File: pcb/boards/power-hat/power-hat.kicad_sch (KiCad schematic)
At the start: 40 parts, among them J1 ISO_A, J2 Raspberry_Pi_GPIO, J3 ISP, J4 FAN, Q1 IRLB8721PBF, Q2 2N7002, Q3 2N7002, U1 TPS54560BDDA, U2 LTV-817S, U3 attiny85, Y1 16Mhz Crystal

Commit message: Power HAT: Initial PCB layout with component placement
PCB Layout:
- 65mm × 56mm board outline (standard Pi HAT)
- 4× M2.5 mounting holes at corners
- 40-pin GPIO header (J2) positioned for Pi stacking
- Power section (U1 TPS54560, L1, capacitors) on left side
- MCU section (U3 ATtiny85, Y1 crystal) in center
- MOSFET power switching (Q1, Q2, Q3) at bottom
- Optocoupler (U2) for ignition detection

Also includes:
- DAC/Amp HAT schematic complete with I2S, I2C, power wiring
- CAN HAT schematic updates
- Layout scripts for automated component placement
- Updated documentation

Co-Authored-By: Claude Opus 4.5 <noreply@anthropic.com>
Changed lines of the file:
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@@
 		(color 0 0 0 0)
 	)
-	(junction
-		(at 422.91 147.32)
-		(diameter 0)
-		(color 0 0 0 0)
-	)
 	(no_connect
 		(at 207.62 152.54)
@@
 	(wire
 		(pts
+			(xy 322.58 511.81) (xy 317.5 511.81)
+		)
+		(stroke
+			(width 0)
+			(type default)
+		)
+	)
+	(wire
+		(pts
 			(xy 172.72 121.92) (xy 182.88 121.92)
 		)
@@
 	(wire
 		(pts
+			(xy 273.05 502.92) (xy 269.24 502.92)
+		)
+		(stroke
+			(width 0)
+			(type default)
+		)
+	)
+	(wire
+		(pts
 			(xy 118.11 702.31) (xy 118.11 701.04)
 		)
@@
 	(wire
 		(pts
-			(xy 436.88 123.19) (xy 444.5 123.19)
+			(xy 273.05 495.3) (xy 274.32 495.3)
 		)
 		(stroke
@@
 	(wire
 		(pts
-			(xy 549.91 510.54) (xy 549.91 508)
+			(xy 436.88 123.19) (xy 444.5 123.19)
 		)
 		(stroke
@@
 	(wire
 		(pts
-			(xy 322.58 511.81) (xy 317.5 511.81)
+			(xy 549.91 510.54) (xy 549.91 508)
 		)
 		(stroke
@@
 	(wire
 		(pts
+			(xy 273.05 501.65) (xy 273.05 502.92)
+		)
+		(stroke
+			(width 0)
+			(type default)
+		)
+	)
+	(wire
+		(pts
 			(xy 628.65 576.58) (xy 628.65 574.04)
 		)
@@
 	(wire
 		(pts
+			(xy 273.05 500.38) (xy 269.24 500.38)
+		)
+		(stroke
+			(width 0)
+			(type default)
+		)
+	)
+	(wire
+		(pts
 			(xy 104.3 334.01) (xy 114.3 334.01)
 		)
@@
 	(wire
 		(pts
-			(xy 183 127.14) (xy 194.92 127.14)
+			(xy 273.05 495.3) (xy 273.05 500.38)
 		)
 		(stroke
@@
 	(wire
 		(pts
-			(xy 549.91 508) (xy 566.42 508)
+			(xy 183 127.14) (xy 194.92 127.14)
 		)
 		(stroke
@@
 	(wire
 		(pts
-			(xy 101.6 321.31) (xy 97.79 321.31)
+			(xy 549.91 508) (xy 566.42 508)
 		)
 		(stroke
@@
 	(wire
 		(pts
-			(xy 381 194.31) (xy 391 194.31)
+			(xy 101.6 321.31) (xy 97.79 321.31)
 		)
 		(stroke
@@
 	(wire
 		(pts
-			(xy 44.45 134.62) (xy 58.42 134.62)
+			(xy 381 194.31) (xy 391 194.31)
 		)
 		(stroke
@@
 	(wire
 		(pts
-			(xy 381 186.69) (xy 376 186.69)
+			(xy 273.05 501.65) (xy 276.86 501.65)
 		)
 		(stroke
@@
 	(wire
 		(pts
-			(xy 38.1 127) (xy 58.42 127)
+			(xy 44.45 134.62) (xy 58.42 134.62)
 		)
 		(stroke
@@
 	(wire
 		(pts
-			(xy 321.31 124.46) (xy 318.77 124.46)
+			(xy 381 186.69) (xy 376 186.69)
 		)
 		(stroke
@@
 	(wire
 		(pts
-			(xy 127 130.81) (xy 137 130.81)
+			(xy 38.1 127) (xy 58.42 127)
 		)
 		(stroke
@@
 	(wire
 		(pts
-			(xy 415.29 147.32) (xy 422.91 147.32)
+			(xy 321.31 124.46) (xy 318.77 124.46)
 		)
 		(stroke
@@
 	(wire
 		(pts
-			(xy 269.24 500.38) (xy 274.32 500.38)
+			(xy 127 130.81) (xy 137 130.81)
 		)
 		(stroke
@@
 	(wire
 		(pts
-			(xy 269.24 502.92) (xy 274.32 502.92)
+			(xy 415.29 147.32) (xy 422.91 147.32)
 		)
 		(stroke
@@
 		)
 	)
+	(global_label "HEARTBEAT_LED"
+		(shape input)
+		(at 274.32 495.3 0)
+		(fields_autoplaced yes)
+		(effects
+			(font
+				(size 1.27 1.27)
+			)
+			(justify left)
+		)
+		(property "Intersheetrefs" "${INTERSHEET_REFS}"
+			(at 274.32 495.3 0)
+			(effects
+				(font
+					(size 1.27 1.27)
+				)
+				(hide yes)
+			)
+		)
+	)
 	(global_label "+5V"
 		(shape passive)
@@
 		)
 	)
+	(global_label "Q2_GATE"
+		(shape input)
+		(at 444.5 194.31 0)
+		(fields_autoplaced yes)
+		(effects
+			(font
+				(size 1.27 1.27)
+			)
+			(justify left)
+		)
+		(property "Intersheetrefs" "${INTERSHEET_REFS}"
+			(at 444.5 194.31 0)
+			(effects
+				(font
+					(size 1.27 1.27)
+				)
+				(hide yes)
+			)
+		)
+	)
 	(global_label "12V_FUSED"
 		(shape input)
@@
 		)
 	)
+	(global_label "R6_OUT"
+		(shape input)
+		(at 322.58 511.81 0)
+		(fields_autoplaced yes)
+		(effects
+			(font
+				(size 1.27 1.27)
+			)
+			(justify left)
+		)
+		(property "Intersheetrefs" "${INTERSHEET_REFS}"
+			(at 322.58 511.81 0)
+			(effects
+				(font
+					(size 1.27 1.27)
+				)
+				(hide yes)
+			)
+		)
+	)
 	(global_label "GND"
 		(shape passive)
@@
 		)
 	)
+	(global_label "TIMER_LED"
+		(shape input)
+		(at 276.86 501.65 0)
+		(fields_autoplaced yes)
+		(effects
+			(font
+				(size 1.27 1.27)
+			)
+			(justify left)
+		)
+		(property "Intersheetrefs" "${INTERSHEET_REFS}"
+			(at 276.86 501.65 0)
+			(effects
+				(font
+					(size 1.27 1.27)
+				)
+				(hide yes)
+			)
+		)
+	)
 	(global_label "GND"
 		(shape input)
@@
 		)
 	)
-	(global_label "HEARTBEAT_LED"
-		(shape input)
-		(at 274.32 500.38 0)
-		(fields_autoplaced yes)
-		(effects
-			(font
-				(size 1.27 1.27)
-			)
-			(justify left)
-		)
-		(property "Intersheetrefs" "${INTERSHEET_REFS}"
-			(at 274.32 500.38 0)
-			(effects
-				(font
-					(size 1.27 1.27)
-				)
-				(hide yes)
-			)
-		)
-	)
-	(global_label "TIMER_LED"
-		(shape input)
-		(at 274.32 502.92 0)
-		(fields_autoplaced yes)
-		(effects
-			(font
-				(size 1.27 1.27)
-			)
-			(justify left)
-		)
-		(property "Intersheetrefs" "${INTERSHEET_REFS}"
-			(at 274.32 502.92 0)
-			(effects
-				(font
-					(size 1.27 1.27)
-				)
-				(hide yes)
-			)
-		)
-	)
-	(global_label "Q2_GATE"
-		(shape input)
-		(at 444.5 194.31 0)
-		(fields_autoplaced yes)
-		(effects
-			(font
-				(size 1.27 1.27)
-			)
-			(justify left)
-		)
-		(property "Intersheetrefs" "${INTERSHEET_REFS}"
-			(at 444.5 194.31 0)
-			(effects
-				(font
-					(size 1.27 1.27)
-				)
-				(hide yes)
-			)
-		)
-	)
-	(global_label "R6_OUT"
-		(shape input)
-		(at 317.5 511.81 0)
-		(fields_autoplaced yes)
-		(effects
-			(font
-				(size 1.27 1.27)
-			)
-			(justify left)
-		)
-		(property "Intersheetrefs" "${INTERSHEET_REFS}"
-			(at 317.5 511.81 0)
-			(effects
-				(font
-					(size 1.27 1.27)
-				)
-				(hide yes)
-			)
-		)
-	)
 	(symbol
 		(lib_id "Device:C")
@@
 		(dnp no)
 		(property "Reference" "R4"
-			(at 317.5 503 0)
+			(at 313.69 501.396 0)
 			(effects
 				(font
@@
 		)
 		(property "Value" "2N7002"
-			(at 381 132 0)
+			(at 373.888 131.318 0)
 			(effects
 				(font
@@
 		(dnp no)
 		(property "Reference" "J2"
-			(at 200 120 0)
+			(at 200.914 116.84 0)
 			(effects
 				(font

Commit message: Power HAT: Add 4-pin PWM fan control (GPIO12/13)
- Upgrade J4 from 2-pin to 4-pin PWM fan connector
- Wire FAN_PWM (GPIO12) for Pi-controlled speed
- Wire FAN_TACH (GPIO13) for RPM feedback
- Add layout_power_hat_v3.py with X735-style 30mm fan placement
- ERC clean: 0 errors, 49 warnings

Co-Authored-By: Claude Opus 4.5 <noreply@anthropic.com>
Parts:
- J4: value FAN -> FAN_4PIN; footprint Connector_PinHeader_2.54mm:PinHeader_1x02_P2.54mm_Vertical -> Connector_PinHeader_2.54mm:PinHeader_1x04_P2.54mm_Vertical; symbol Connector_Generic:Conn_01x02 -> Connector_Generic:Conn_01x04
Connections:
- net FAN+: now also J4.2 (Pin_2); no longer J4.1 (Pin_1)
- net FAN-: no longer J4.2 (Pin_2)
- net FAN_PWM: now also J2.32 (Pin_32), J4.4 (Pin_4)
- net GND: now also J4.1 (Pin_1)
- net FAN_TACH: now reaches J2.33 (Pin_33)
- net FAN_TACH: now also J4.3 (Pin_3)
- no-connect marks 38 -> 36
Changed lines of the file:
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@@
 		(color 0 0 0 0)
 	)
+	(junction
+		(at 628.65 574.04)
+		(diameter 0)
+		(color 0 0 0 0)
+	)
 	(no_connect
 		(at 207.62 152.54)
@@
 	)
 	(no_connect
-		(at 207.62 165.24)
-	)
-	(no_connect
 		(at 194.92 152.54)
 	)
@@
 	)
 	(no_connect
-		(at 194.92 167.78)
-	)
-	(no_connect
 		(at 207.62 172.86)
 	)
@@
 	(wire
 		(pts
+			(xy 623.57 572.77) (xy 626.11 572.77)
+		)
+		(stroke
+			(width 0)
+			(type default)
+		)
+	)
+	(wire
+		(pts
 			(xy 114.3 695.96) (xy 119.38 695.96)
 		)
@@
 	(wire
 		(pts
+			(xy 628.65 574.04) (xy 629.92 574.04)
+		)
+		(stroke
+			(width 0)
+			(type default)
+		)
+	)
+	(wire
+		(pts
 			(xy 572.77 501.65) (xy 574.04 501.65)
 		)
@@
 	(wire
 		(pts
-			(xy 626.11 567.69) (xy 623.57 567.69)
+			(xy 621.03 576.58) (xy 629.92 576.58)
+		)
+		(stroke
+			(width 0)
+			(type default)
+		)
+	)
+	(wire
+		(pts
+			(xy 626.11 562.61) (xy 614.68 562.61)
 		)
 		(stroke
@@
 	(wire
 		(pts
+			(xy 207.62 165.24) (xy 212.62 165.24)
+		)
+		(stroke
+			(width 0)
+			(type default)
+		)
+	)
+	(wire
+		(pts
 			(xy 760.73 820.42) (xy 765.81 820.42)
 		)
@@
 	(wire
 		(pts
+			(xy 626.11 574.04) (xy 628.65 574.04)
+		)
+		(stroke
+			(width 0)
+			(type default)
+		)
+	)
+	(wire
+		(pts
 			(xy 250.19 123.19) (xy 250.19 127)
 		)
@@
 	(wire
 		(pts
+			(xy 621.03 568.96) (xy 629.92 568.96)
+		)
+		(stroke
+			(width 0)
+			(type default)
+		)
+	)
+	(wire
+		(pts
 			(xy 207.62 162.7) (xy 212.62 162.7)
 		)
@@
 	(wire
 		(pts
-			(xy 207.62 129.68) (xy 212.62 129.68)
+			(xy 194.92 167.78) (xy 189.92 167.78)
 		)
 		(stroke
@@
 	(wire
 		(pts
-			(xy 127 349.25) (xy 127 350.52)
+			(xy 207.62 129.68) (xy 212.62 129.68)
 		)
 		(stroke
@@
 	(wire
 		(pts
-			(xy 137.16 703.58) (xy 137.16 701.04)
+			(xy 127 349.25) (xy 127 350.52)
 		)
 		(stroke
@@
 	(wire
 		(pts
-			(xy 623.57 576.58) (xy 628.65 576.58)
+			(xy 137.16 703.58) (xy 137.16 701.04)
 		)
 		(stroke
@@
 	(wire
 		(pts
-			(xy 626.11 567.69) (xy 626.11 571.5)
+			(xy 626.11 562.61) (xy 626.11 571.5)
 		)
 		(stroke
@@
 	(wire
 		(pts
-			(xy 628.65 574.04) (xy 629.92 574.04)
+			(xy 581.66 513.08) (xy 574.04 513.08)
 		)
 		(stroke
@@
 	(wire
 		(pts
-			(xy 581.66 513.08) (xy 574.04 513.08)
+			(xy 762 833.12) (xy 762 829.31)
 		)
 		(stroke
@@
 	(wire
 		(pts
-			(xy 762 833.12) (xy 762 829.31)
+			(xy 207.62 142.38) (xy 212.62 142.38)
 		)
 		(stroke
@@
 	(wire
 		(pts
-			(xy 207.62 142.38) (xy 212.62 142.38)
+			(xy 273.05 495.3) (xy 273.05 500.38)
 		)
 		(stroke
@@
 	(wire
 		(pts
-			(xy 273.05 495.3) (xy 273.05 500.38)
+			(xy 183 127.14) (xy 194.92 127.14)
 		)
 		(stroke
@@
 	(wire
 		(pts
-			(xy 183 127.14) (xy 194.92 127.14)
+			(xy 549.91 508) (xy 566.42 508)
 		)
 		(stroke
@@
 	(wire
 		(pts
-			(xy 549.91 508) (xy 566.42 508)
+			(xy 101.6 321.31) (xy 97.79 321.31)
 		)
 		(stroke
@@
 	(wire
 		(pts
-			(xy 101.6 321.31) (xy 97.79 321.31)
+			(xy 621.03 567.69) (xy 621.03 568.96)
 		)
 		(stroke
@@
 	(wire
 		(pts
+			(xy 626.11 572.77) (xy 626.11 574.04)
+		)
+		(stroke
+			(width 0)
+			(type default)
+		)
+	)
+	(wire
+		(pts
 			(xy 44.45 134.62) (xy 58.42 134.62)
 		)
@@
 		)
 	)
+	(global_label "FAN_TACH"
+		(shape passive)
+		(at 623.57 572.77 180)
+		(effects
+			(font
+				(size 1.27 1.27)
+			)
+			(justify right)
+		)
+		(property "Intersheetrefs" "${INTERSHEET_REFS}"
+			(at 623.57 572.77 0)
+			(effects
+				(font
+					(size 1.27 1.27)
+				)
+				(hide yes)
+			)
+		)
+	)
 	(global_label "GATE_CTRL"
 		(shape input)
@@
 		)
 	)
+	(global_label "FAN_PWM"
+		(shape passive)
+		(at 212.62 165.24 180)
+		(effects
+			(font
+				(size 1.27 1.27)
+			)
+			(justify right)
+		)
+		(property "Intersheetrefs" "${INTERSHEET_REFS}"
+			(at 212.62 165.24 0)
+			(effects
+				(font
+					(size 1.27 1.27)
+				)
+				(hide yes)
+			)
+		)
+	)
 	(global_label "GND"
 		(shape input)
@@
 		)
 	)
-	(global_label "XTAL1"
+	(global_label "GND"
+		(shape passive)
+		(at 621.03 567.69 180)
+		(effects
+			(font
+				(size 1.27 1.27)
+			)
+			(justify right)
+		)
+		(property "Intersheetrefs" "${INTERSHEET_REFS}"
+			(at 621.03 567.69 0)
+			(effects
+				(font
+					(size 1.27 1.27)
+				)
+				(hide yes)
+			)
+		)
+	)
+	(global_label "FAN_TACH"
 		(shape input)
-		(at 571.5 758.19 0)
-		(fields_autoplaced yes)
+		(at 189.92 167.78 0)
 		(effects
 			(font
@@
 		)
 		(property "Intersheetrefs" "${INTERSHEET_REFS}"
-			(at 571.5 758.19 0)
+			(at 189.92 167.78 0)
 			(effects
 				(font
@@
 		)
 	)
-	(global_label "FAN-"
+	(global_label "XTAL1"
 		(shape input)
-		(at 623.57 576.58 0)
+		(at 571.5 758.19 0)
 		(fields_autoplaced yes)
 		(effects
@@
 		)
 		(property "Intersheetrefs" "${INTERSHEET_REFS}"
-			(at 623.57 576.58 0)
+			(at 571.5 758.19 0)
 			(effects
 				(font
@@
 		)
 	)
+	(global_label "FAN_PWM"
+		(shape passive)
+		(at 621.03 576.58 180)
+		(effects
+			(font
+				(size 1.27 1.27)
+			)
+			(justify right)
+		)
+		(property "Intersheetrefs" "${INTERSHEET_REFS}"
+			(at 621.03 576.58 0)
+			(effects
+				(font
+					(size 1.27 1.27)
+				)
+				(hide yes)
+			)
+		)
+	)
 	(global_label "XTAL2"
 		(shape input)
@@
 	(global_label "FAN+"
 		(shape passive)
-		(at 623.57 567.69 0)
+		(at 614.68 562.61 0)
 		(effects
 			(font
@@
 		)
 		(property "Intersheetrefs" "${INTERSHEET_REFS}"
-			(at 623.57 567.69 0)
+			(at 614.68 562.61 0)
 			(effects
 				(font
@@
 	)
 	(symbol
-		(lib_id "Connector_Generic:Conn_01x02")
+		(lib_id "Connector_Generic:Conn_01x04")
 		(at 635 571.5 0)
 		(unit 1)
@@
 			)
 		)
-		(property "Value" "FAN"
+		(property "Value" "FAN_4PIN"
 			(at 635 576.5 0)
 			(effects
@@
 			)
 		)
-		(property "Footprint" "Connector_PinHeader_2.54mm:PinHeader_1x02_P2.54mm_Vertical"
+		(property "Footprint" "Connector_PinHeader_2.54mm:PinHeader_1x04_P2.54mm_Vertical"
 			(at 635 571.5 0)
 			(effects
@@
 		(pin "1"
 		)
+		(pin "4"
+		)
+		(pin "3"
+		)
 		(instances

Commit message: Power HAT: Fix ERC errors - 0 errors, 55 warnings
Manual schematic fixes:
- J1: Updated to Molex Micro-Fit 3.0 6-pin connector
- C6: Fixed short - changed bottom pin from +3.3V to GND
- C8: Reconnected as feedforward cap (+5V to U1-FB)
- C9: Fixed net label from 12V_IGN to 12V_FUSED
- R6: Fixed label to 12V_IGN to GND (ignition divider)
- D1 (TVS): Moved away from J2, reconnected 12V_FUSED to GND
- Removed stray 12V_IGN label hidden behind U1
- Added PWR_FLAG to 12V_FUSED and +3.3V nets

All critical ERC errors resolved. Remaining 55 warnings are
non-critical (off-grid endpoints, dangling labels, same local/global).

Co-Authored-By: Claude Opus 4.5 <noreply@anthropic.com>
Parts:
- removed J1: ISO_A, Connector_Molex:Molex_Mini-Fit_Jr_5566-08A_2x04_P4.20mm_Vertical, symbol Connector_Generic:Conn_01x08
- added J1: Micro-Fit_3.0, Connector_Molex:Molex_Micro-Fit_3.0_43045-0612_2x03_P3.00mm_Vertical, symbol Connector_Generic:Conn_02x03_Odd_Even
- C8: value 10uF -> 47pF
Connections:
- net +3.3V: no longer C6.2, J2.1 (Pin_1)
- net +5V: now also C8.1
- net 12V_ACC: now also J1.3 (Pin_3)
- net 12V_FUSED: now also J2.1 (Pin_1); no longer D2.2 (A), F1.1, R6.1, U1.3 (EN)
- net GND: now also C6.2, J1.4 (Pin_4), J1.5 (Pin_5), J1.6 (Pin_6); no longer C8.2
- net XTAL2: no longer C8.1
- new net 12V_IGN: D2.2 (A), F1.1, J1.1 (Pin_1), J1.2 (Pin_2), R6.1, U1.3 (EN)
- new net U1-FB: C8.2
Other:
- moved on the sheet: D1

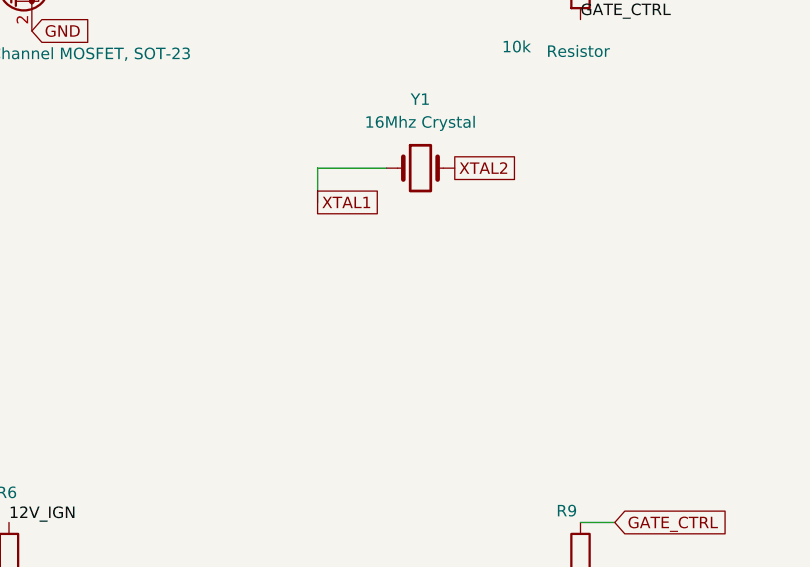
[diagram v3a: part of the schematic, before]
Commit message: Power HAT PCB: DRC clean routing via FreeRouting
- Complete auto-routing with FreeRouting (power-hat.ses)
- All DRC errors resolved (120 warnings, 0 errors)
- Fixed J2 +5V/GND short, edge clearance, R_COMP1 clearance
- Added keepout zone for fan cutout area
- Added STATUS.md with next steps (power trace widths need widening)

TODO: Widen power traces (12V_FUSED, +5V, GND, U1_SW) from 0.2mm to 1.5mm

Co-Authored-By: Claude Opus 4.5 <noreply@anthropic.com>
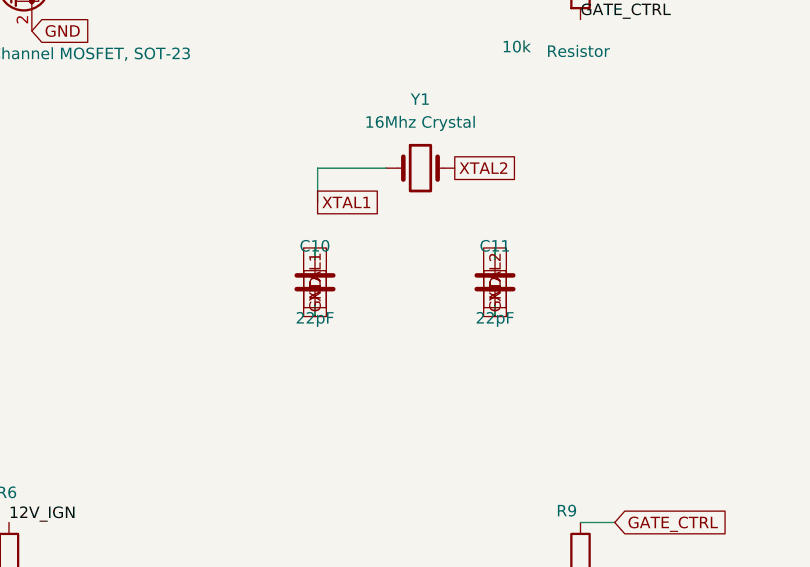
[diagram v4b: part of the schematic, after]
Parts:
- added C10, C11: 22pF, Capacitor_SMD:C_0805_2012Metric, symbol Device:C
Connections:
- net GND: now also C10.2, C11.2
- net XTAL1: now also C10.1
- net XTAL2: now also C11.1
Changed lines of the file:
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@@
 	)
 	(embedded_fonts no)
+	(symbol
+		(lib_id "Device:C")
+		(at 415.0 160.0 0)
+		(unit 1)
+		(exclude_from_sim no)
+		(in_bom yes)
+		(on_board yes)
+		(dnp no)
+		(property "Reference" "C10"
+			(at 415.0 156.0 0)
+			(effects
+				(font
+					(size 1.27 1.27)
+				)
+			)
+		)
+		(property "Value" "22pF"
+			(at 415.0 164.0 0)
+			(effects
+				(font
+					(size 1.27 1.27)
+				)
+			)
+		)
+		(property "Footprint" "Capacitor_SMD:C_0805_2012Metric"
+			(at 415.0 160.0 0)
+			(effects
+				(font
+					(size 1.27 1.27)
+				)
+				(hide yes)
+			)
+		)
+		(property "Datasheet" "~"
+			(at 415.0 160.0 0)
+			(effects
+				(font
+					(size 1.27 1.27)
+				)
+				(hide yes)
+			)
+		)
+		(property "Description" "Crystal load capacitor"
+			(at 415.0 160.0 0)
+			(effects
+				(font
+					(size 1.27 1.27)
+				)
+				(hide yes)
+			)
+		)
+		(pin "1"
+		)
+		(pin "2"
+		)
+		(instances
+			(project "power-hat"
+				(path "/29b54e26-6a52-4b51-8c39-076401b40ee9"
+					(reference "C10")
+					(unit 1)
+				)
+			)
+		)
+	)
+	(symbol
+		(lib_id "Device:C")
+		(at 435.0 160.0 0)
+		(unit 1)
+		(exclude_from_sim no)
+		(in_bom yes)
+		(on_board yes)
+		(dnp no)
+		(property "Reference" "C11"
+			(at 435.0 156.0 0)
+			(effects
+				(font
+					(size 1.27 1.27)
+				)
+			)
+		)
+		(property "Value" "22pF"
+			(at 435.0 164.0 0)
+			(effects
+				(font
+					(size 1.27 1.27)
+				)
+			)
+		)
+		(property "Footprint" "Capacitor_SMD:C_0805_2012Metric"
+			(at 435.0 160.0 0)
+			(effects
+				(font
+					(size 1.27 1.27)
+				)
+				(hide yes)
+			)
+		)
+		(property "Datasheet" "~"
+			(at 435.0 160.0 0)
+			(effects
+				(font
+					(size 1.27 1.27)
+				)
+				(hide yes)
+			)
+		)
+		(property "Description" "Crystal load capacitor"
+			(at 435.0 160.0 0)
+			(effects
+				(font
+					(size 1.27 1.27)
+				)
+				(hide yes)
+			)
+		)
+		(pin "1"
+		)
+		(pin "2"
+		)
+		(instances
+			(project "power-hat"
+				(path "/29b54e26-6a52-4b51-8c39-076401b40ee9"
+					(reference "C11")
+					(unit 1)
+				)
+			)
+		)
+	)
+	(global_label "XTAL1"
+		(shape passive)
+		(at 415.0 156.19 270)
+		(effects
+			(font
+				(size 1.27 1.27)
+			)
+			(justify right)
+		)
+		(property "Intersheetrefs" "${INTERSHEET_REFS}"
+			(at 415.0 156.19 0)
+			(effects
+				(font
+					(size 1.27 1.27)
+				)
+				(hide yes)
+			)
+		)
+	)
+	(global_label "GND"
+		(shape passive)
+		(at 415.0 163.81 270)
+		(effects
+			(font
+				(size 1.27 1.27)
+			)
+			(justify left)
+		)
+		(property "Intersheetrefs" "${INTERSHEET_REFS}"
+			(at 415.0 163.81 0)
+			(effects
+				(font
+					(size 1.27 1.27)
+				)
+				(hide yes)
+			)
+		)
+	)
+	(global_label "XTAL2"
+		(shape passive)
+		(at 435.0 156.19 270)
+		(effects
+			(font
+				(size 1.27 1.27)
+			)
+			(justify right)
+		)
+		(property "Intersheetrefs" "${INTERSHEET_REFS}"
+			(at 435.0 156.19 0)
+			(effects
+				(font
+					(size 1.27 1.27)
+				)
+				(hide yes)
+			)
+		)
+	)
+	(global_label "GND"
+		(shape passive)
+		(at 435.0 163.81 270)
+		(effects
+			(font
+				(size 1.27 1.27)
+			)
+			(justify left)
+		)
+		(property "Intersheetrefs" "${INTERSHEET_REFS}"
+			(at 435.0 163.81 0)
+			(effects
+				(font
+					(size 1.27 1.27)
+				)
+				(hide yes)
+			)
+		)
+	)
+	(wire
+		(pts
+			(xy 415.0 156.19) (xy 415.0 157.46)
+		)
+		(stroke
+			(width 0)
+			(type default)
+		)
+	)
+	(wire
+		(pts
+			(xy 415.0 162.54) (xy 415.0 163.81)
+		)
+		(stroke
+			(width 0)
+			(type default)
+		)
+	)
+	(wire
+		(pts
+			(xy 435.0 156.19) (xy 435.0 157.46)
+		)
+		(stroke
+			(width 0)
+			(type default)
+		)
+	)
+	(wire
+		(pts
+			(xy 435.0 162.54) (xy 435.0 163.81)
+		)
+		(stroke
+			(width 0)
+			(type default)
+		)
+	)
 )
